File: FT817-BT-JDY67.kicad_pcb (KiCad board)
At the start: 2 copper layers, 93.3 x 33.7 mm, 34 parts, among them J1009 Mini-DIN-8PR, J1010 Mini-DIN-6PR, Q1 2N7002, Q2 TP0610, U1 JDY-67 Bluetooth Module, U2 LM1117MP-5.0

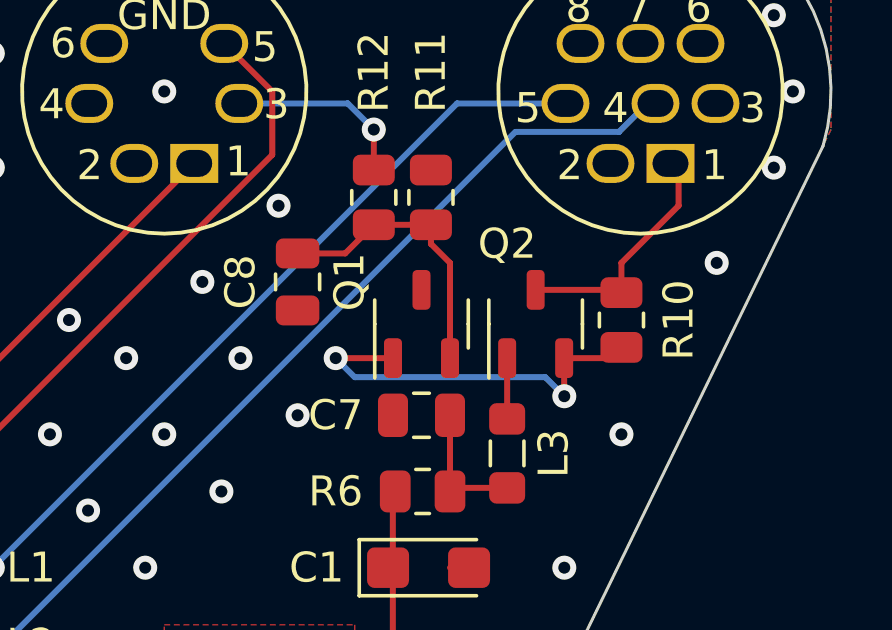
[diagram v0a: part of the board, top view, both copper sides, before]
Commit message: Fixed 2N7002 Footprint
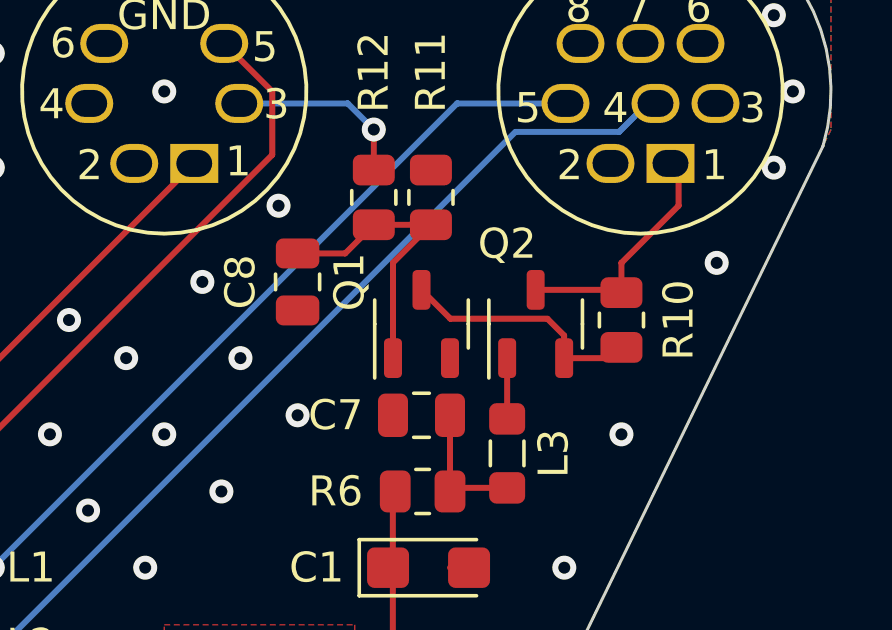
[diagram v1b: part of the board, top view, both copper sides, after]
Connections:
- Q1 pad 1: Net-(Q1-D) -> Net-(Q1-G)
- Q1 pad 2: Net-(Q1-G) -> GND
- Q1 pad 3: GND -> Net-(Q1-D)
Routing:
- net Net-(Q1-D): track 13.5 -> 8.33 mm, vias 2 -> 0
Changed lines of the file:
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@@
       (usegerberextensions false)
       (usegerberattributes true)
-      (usegerberadvancedattributes true)
+      (usegerberadvancedattributes false)
       (creategerberjobfile true)
       (dashed_line_dash_ratio 12.000000)
@@
       (stroke (width 0.1) (type solid)) (layer "F.Fab"))
     (pad "1" smd roundrect (at -1.1375 -0.95 90) (size 1.325 0.6) (layers "F.Cu" "F.Paste" "F.Mask") (roundrect_rratio 0.25)
-      (net 40 "Net-(Q1-D)") (pinfunction "D") (pintype "passive"))
-    (pad "2" smd roundrect (at -1.1375 0.95 90) (size 1.325 0.6) (layers "F.Cu" "F.Paste" "F.Mask") (roundrect_rratio 0.25)
       (net 38 "Net-(Q1-G)") (pinfunction "G") (pintype "input"))
-    (pad "3" smd roundrect (at 1.1375 0 90) (size 1.325 0.6) (layers "F.Cu" "F.Paste" "F.Mask") (roundrect_rratio 0.25)
+    (pad "2" smd roundrect (at -1.1375 0.95 90) (size 1.325 0.6) (layers "F.Cu" "F.Paste" "F.Mask") (roundrect_rratio 0.25)
       (net 24 "GND") (pinfunction "S") (pintype "passive"))
+    (pad "3" smd roundrect (at 1.1375 0 90) (size 1.325 0.6) (layers "F.Cu" "F.Paste" "F.Mask") (roundrect_rratio 0.25)
+      (net 40 "Net-(Q1-D)") (pinfunction "D") (pintype "passive"))
     (model "${KICAD6_3DMODEL_DIR}/Package_TO_SOT_SMD.3dshapes/SOT-23-3.wrl"
       (offset (xyz 0 0 0))
@@
   (gr_arc (start 154.305 64.77) (mid 154.862962 63.422962) (end 156.21 62.865)
     (stroke (width 0.1) (type default)) (layer "Edge.Cuts"))
-  (image (at 143.51 79.375) (layer "User.2") (scale 0.229514)
+  (image (at 143.51 80.01) (layer "User.2") (scale 0.229514)
     (data
       iVBORw0KGgoAAAANSUhEUgAADOQAAAOgCAIAAACoDt/6AAAAA3NCSVQICAjb4U/gAAAACXBIWXMA
@@
     )
   )
-  (image (at 143.51 80.01) (layer "User.2") (scale 0.229514)
+  (image (at 143.51 79.375) (layer "User.2") (scale 0.229514)
     (data
       iVBORw0KGgoAAAANSUhEUgAADOQAAAOgCAIAAACoDt/6AAAAA3NCSVQICAjb4U/gAAAACXBIWXMA
@@
   (segment (start 171.45 80.01) (end 171.45 82.55) (width 0.2) (layer "F.Cu") (net 37))
   (segment (start 173.355 82.43) (end 171.57 82.43) (width 0.2) (layer "F.Cu") (net 37))
-  (segment (start 171.45 74.93) (end 171.45 78.105) (width 0.2) (layer "F.Cu") (net 38))
+  (segment (start 170.815 73.66) (end 169.55 74.925) (width 0.2) (layer "F.Cu") (net 38))
   (segment (start 166.37 74.615) (end 167.955 74.615) (width 0.2) (layer "F.Cu") (net 38))
-  (segment (start 170.815 73.66) (end 170.815 74.295) (width 0.2) (layer "F.Cu") (net 38))
-  (segment (start 170.815 74.295) (end 171.45 74.93) (width 0.2) (layer "F.Cu") (net 38))
   (segment (start 167.955 74.615) (end 168.91 73.66) (width 0.2) (layer "F.Cu") (net 38))
+  (segment (start 169.55 74.925) (end 169.55 78.105) (width 0.2) (layer "F.Cu") (net 38))
   (segment (start 170.815 73.66) (end 168.91 73.66) (width 0.2) (layer "F.Cu") (net 38))
   (segment (start 173.355 78.105) (end 173.355 80.13) (width 0.2) (layer "F.Cu") (net 39))
-  (segment (start 169.55 78.105) (end 167.64 78.105) (width 0.2) (layer "F.Cu") (net 40))
-  (segment (start 175.255 79.37) (end 175.255 78.105) (width 0.2) (layer "F.Cu") (net 40))
-  (segment (start 175.26 79.375) (end 175.255 79.37) (width 0.2) (layer "F.Cu") (net 40))
+  (segment (start 174.6975 76.7925) (end 171.4625 76.7925) (width 0.2) (layer "F.Cu") (net 40))
+  (segment (start 171.4625 76.7925) (end 170.5 75.83) (width 0.2) (layer "F.Cu") (net 40))
+  (segment (start 175.255 78.105) (end 175.255 77.35) (width 0.2) (layer "F.Cu") (net 40))
+  (segment (start 175.255 77.35) (end 174.6975 76.7925) (width 0.2) (layer "F.Cu") (net 40))
   (segment (start 175.255 78.105) (end 177.4425 78.105) (width 0.2) (layer "F.Cu") (net 40))
-  (via (at 167.64 78.105) (size 0.8) (drill 0.4) (layers "F.Cu" "B.Cu") (net 40))
-  (via (at 175.26 79.375) (size 0.8) (drill 0.4) (layers "F.Cu" "B.Cu") (net 40))
-  (segment (start 175.26 79.375) (end 174.625 78.74) (width 0.2) (layer "B.Cu") (net 40))
-  (segment (start 168.275 78.74) (end 167.64 78.105) (width 0.2) (layer "B.Cu") (net 40))
-  (segment (start 174.625 78.74) (end 168.275 78.74) (width 0.2) (layer "B.Cu") (net 40))
   (zone (net 36) (net_name "5V") (layer "F.Cu") (hatch full 0.2)
     (priority 1)
